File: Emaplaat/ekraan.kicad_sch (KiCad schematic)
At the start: 37 parts, among them IC1 74HC595PW-Q100,118, IC10 1EDN7550BXTSA1, IC11 1EDN7550BXTSA1, IC3 1EDN7550BXTSA1, IC6 1EDN7550BXTSA1, IC7 1EDN7550BXTSA1, IC8 1EDN7550BXTSA1, IC9 1EDN7550BXTSA1, U1 1EDN7550BXTSA1

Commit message: qwerghhgfdsdfghqwerghhgfdsdfghjj
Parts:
- removed C1, C16, C18, C2, C5, C6, C9: 22u, symbol Device:C
- removed C15, C17, C19, C3, C4, C7, C8: 20u, Capacitor_SMD:C_0201_0603Metric, symbol Device:C
- removed IC10, IC11, IC3, IC6, IC7, IC8, IC9: 1EDN7550BXTSA1, SOT95P280X145-6N, symbol 1EDN7550BXTSA1:1EDN7550BXTSA1
- removed R10, R11, R12, R13, R14, R15, R16, R17, R3, R4, R9: 33k, symbol Device:R
- removed U1: 1EDN7550BXTSA1, dot_flipper:7_flip_dots, symbol flipdot_7xarray:flipdot_7xarray
- added C31, C33, C35, C37, C39, C41, C49, C51, C53, C55, C57, C59: 47u, symbol Device:C
- added C32, C34, C36, C38, C40, C42, C50, C52, C54, C56, C58, C60: 100u, symbol Device:C
- added IC11, IC12, IC13, IC14, IC15, IC17, IC18, IC19, IC20, IC21, IC22: 74HC595PW-Q100,118, SOP65P640X110-16N, symbol 74HC595PW-Q100_118:74HC595PW-Q100,118
- added R21, R22: 10k, symbol Device:R
- R18, R19, R20: value 33k -> 10k
- renumbered IC1 to IC10
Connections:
- net 1D+ is gone; now on net DS: R18.2
- net 1E+ is gone; now on net SHCP: R20.2
- net 1E- is gone; now on net STCP: R19.2
- net 3V3: now also C31.1, C32.1, C33.1, C34.1, C35.1, C36.1, C37.1, C38.1, C39.1, C40.1, C41.1, C42.1, C49.1, C50.1, C51.1, C52.1, C53.1, C54.1, C55.1, C56.1, C57.1, C58.1, C59.1, C60.1, IC11.16 (VCC), IC12.16 (VCC), IC13.16 (VCC), IC14.16 (VCC), IC15.16 (VCC), IC17.16 (VCC), IC18.16 (VCC), IC19.16 (VCC), IC20.16 (VCC), IC21.16 (VCC), IC22.16 (VCC), R21.2, R22.2
- net AGND: now also R18.1, R19.1, R20.1, C31.2, C32.2, C33.2, C34.2, C35.2, C36.2, C37.2, C38.2, C39.2, C40.2, C41.2, C42.2, C49.2, C50.2, C51.2, C52.2, C53.2, C54.2, C55.2, C56.2, C57.2, C58.2, C59.2, C60.2, IC11.8 (GND), IC12.8 (GND), IC13.8 (GND), IC14.8 (GND), IC15.8 (GND), IC17.8 (GND), IC18.8 (GND), IC19.8 (GND), IC20.8 (GND), IC21.8 (GND), IC22.8 (GND), IC22.9 (Q7S)
- net 1-: now reaches IC10.1 (Q1)
- net !MR: now reaches IC10.10 (~{MR})
- net !MR: now also IC11.10 (~{MR}), IC12.10 (~{MR}), IC13.10 (~{MR}), IC14.10 (~{MR}), IC15.10 (~{MR}), IC17.10 (~{MR}), IC18.10 (~{MR}), IC19.10 (~{MR}), IC20.10 (~{MR}), IC21.10 (~{MR}), IC22.10 (~{MR}), R21.1
- net SHCP: now reaches IC10.11 (SHCP)
- net SHCP: now also IC11.11 (SHCP), IC12.11 (SHCP), IC13.11 (SHCP), IC14.11 (SHCP), IC15.11 (SHCP), IC17.11 (SHCP), IC18.11 (SHCP), IC19.11 (SHCP), IC20.11 (SHCP), IC21.11 (SHCP), IC22.11 (SHCP)
- net STCP: now reaches IC10.12 (STCP)
- net STCP: now also IC11.12 (STCP), IC12.12 (STCP), IC13.12 (STCP), IC14.12 (STCP), IC15.12 (STCP), IC17.12 (STCP), IC18.12 (STCP), IC19.12 (STCP), IC20.12 (STCP), IC21.12 (STCP), IC22.12 (STCP)
- net !OE: now reaches IC10.13 (~{OE})
- net !OE: now also IC11.13 (~{OE}), IC12.13 (~{OE}), IC13.13 (~{OE}), IC14.13 (~{OE}), IC15.13 (~{OE}), IC17.13 (~{OE}), IC18.13 (~{OE}), IC19.13 (~{OE}), IC20.13 (~{OE}), IC21.13 (~{OE}), IC22.13 (~{OE}), R22.1
- net DS: now reaches IC10.14 (DS)
- net 1+: now reaches IC10.15 (Q0)
- net 2+: now reaches IC10.2 (Q2)
- net 2-: now reaches IC10.3 (Q3)
- net 3+: now reaches IC10.4 (Q4)
- net 3-: now reaches IC10.5 (Q5)
- net 4+: now reaches IC10.6 (Q6)
- net 4-: now reaches IC10.7 (Q7)
- net at IC10.9 (Q7S): now also IC13.14 (DS)
- new net: IC14.9 (Q7S), IC18.14 (DS)
- new net: IC18.9 (Q7S), IC21.14 (DS)
- new net: IC11.9 (Q7S), IC14.14 (DS)
- new net: IC13.9 (Q7S), IC17.14 (DS)
- new net: IC17.9 (Q7S), IC20.14 (DS)
- new net: IC12.14 (DS), IC21.9 (Q7S)
- new net: IC12.9 (Q7S), IC15.14 (DS)
- new net: IC15.9 (Q7S), IC19.14 (DS)
- new net: IC19.9 (Q7S), IC22.14 (DS)
- new net: IC11.14 (DS), IC20.9 (Q7S)
- new net 10+: IC11.2 (Q2)
- new net 10-: IC11.3 (Q3)
- new net 11+: IC11.4 (Q4)
- new net 11-: IC11.5 (Q5)
- new net 12+: IC11.6 (Q6)
- new net 12-: IC11.7 (Q7)
- new net 13+: IC14.15 (Q0)
- new net 13-: IC14.1 (Q1)
- new net 14+: IC14.2 (Q2)
- new net 14-: IC14.3 (Q3)
- new net 15+: IC14.4 (Q4)
- new net 15-: IC14.5 (Q5)
- new net 16+: IC14.6 (Q6)
- new net 16-: IC14.7 (Q7)
- new net 17+: IC12.15 (Q0)
- new net 17-: IC12.1 (Q1)
- new net 18+: IC12.2 (Q2)
- new net 18-: IC12.3 (Q3)
- new net 19+: IC12.4 (Q4)
- new net 19-: IC12.5 (Q5)
- new net 20+: IC12.6 (Q6)
- new net 20-: IC12.7 (Q7)
- new net 21+: IC15.15 (Q0)
- new net 21-: IC15.1 (Q1)
- new net 22+: IC15.2 (Q2)
- new net 22-: IC15.3 (Q3)
- new net 23+: IC15.4 (Q4)
- new net 23-: IC15.5 (Q5)
- new net 24+: IC15.6 (Q6)
- new net 24-: IC15.7 (Q7)
- new net 25+: IC17.15 (Q0)
- new net 25-: IC17.1 (Q1)
- new net 26+: IC17.2 (Q2)
- new net 26-: IC17.3 (Q3)
- new net 27+: IC17.4 (Q4)
- new net 27-: IC17.5 (Q5)
- new net 28+: IC17.6 (Q6)
- new net 28-: IC17.7 (Q7)
- new net 29+: IC20.15 (Q0)
- new net 29-: IC20.1 (Q1)
- new net 30+: IC20.2 (Q2)
- new net 30-: IC20.3 (Q3)
- new net 31+: IC20.4 (Q4)
- new net 31-: IC20.5 (Q5)
- new net 32+: IC20.6 (Q6)
- new net 32-: IC20.7 (Q7)
- new net 33+: IC18.15 (Q0)
- new net 33-: IC18.1 (Q1)
- new net 34+: IC18.2 (Q2)
- new net 34-: IC18.3 (Q3)
- new net 35+: IC18.4 (Q4)
- new net 35-: IC18.5 (Q5)
- new net 36+: IC18.6 (Q6)
- new net 36-: IC18.7 (Q7)
- new net 37+: IC21.15 (Q0)
- new net 37-: IC21.1 (Q1)
- new net 38+: IC21.2 (Q2)
- new net 38-: IC21.3 (Q3)
- new net 39+: IC21.4 (Q4)
- new net 39-: IC21.5 (Q5)
- new net 40+: IC21.6 (Q6)
- new net 40-: IC21.7 (Q7)
- new net 41+: IC19.15 (Q0)
- new net 41-: IC19.1 (Q1)
- new net 42+: IC19.2 (Q2)
- new net 42-: IC19.3 (Q3)
- new net 43+: IC19.4 (Q4)
- new net 43-: IC19.5 (Q5)
- new net 44+: IC19.6 (Q6)
- new net 44-: IC19.7 (Q7)
- new net 45+: IC22.15 (Q0)
- new net 45-: IC22.1 (Q1)
- new net 46+: IC22.2 (Q2)
- new net 46-: IC22.3 (Q3)
- new net 47+: IC22.4 (Q4)
- new net 47-: IC22.5 (Q5)
- new net 48+: IC22.6 (Q6)
- new net 48-: IC22.7 (Q7)
- new net 5+: IC13.15 (Q0)
- new net 5-: IC13.1 (Q1)
- new net 6+: IC13.2 (Q2)
- new net 6-: IC13.3 (Q3)
- new net 7+: IC13.4 (Q4)
- new net 7-: IC13.5 (Q5)
- new net 8+: IC13.6 (Q6)
- new net 8-: IC13.7 (Q7)
- new net 9+: IC11.15 (Q0)
- new net 9-: IC11.1 (Q1)
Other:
- added sheet array (array.kicad_sch)
- added sheet array1 (array.kicad_sch)
- added sheet array2 (array.kicad_sch)
- added sheet array3 (array.kicad_sch)
- added sheet array4 (array.kicad_sch)
- added sheet array5 (array.kicad_sch)
- added sheet array6 (array.kicad_sch)
- note added: "!MR ja !OE tõmmatud üles, ülejäänud sisendid tõmmatud alla"
- note added: "6 nihkeregistrit kontrollimaks 48 flipdot-i"
- note added: "7x7 flipdot-i"
- moved on the sheet: IC10

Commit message: ketamine addict
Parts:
- removed R18, R19, R20, R21, R22: 10k, symbol Device:R
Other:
- sheet array ports: added none; removed 12V, PGND
- sheet array1 ports: added none; removed 12V, PGND
- sheet array2 ports: added none; removed 12V, PGND
- sheet array3 ports: added none; removed 12V, PGND
- sheet array4 ports: added none; removed 12V, PGND
- sheet array5 ports: added none; removed 12V, PGND
- sheet array6 ports: added none; removed 12V, PGND
- note added: "ühendused"
- note removed: "!MR ja !OE tõmmatud üles, ülejäänud sisendid tõmmatud alla"
- moved on the sheet: C31, C32, C33, C34, C35, C36, C37, C38, C39, C40, C41, C42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

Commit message: T________T Heiki Tammemägi
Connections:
- net AGND renamed GND

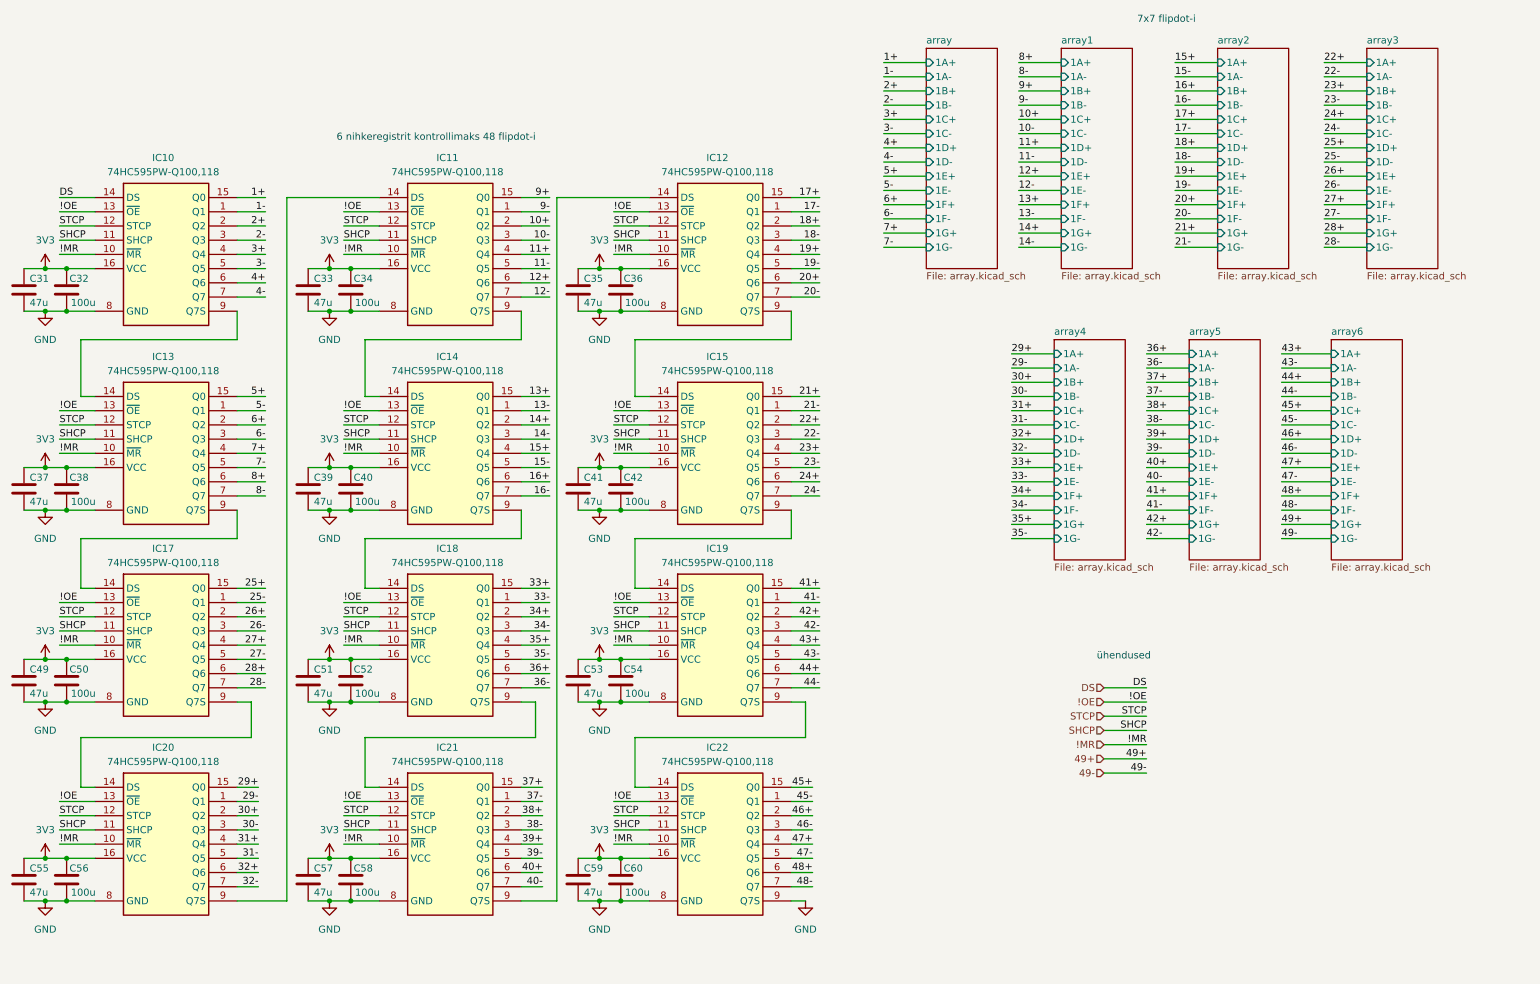
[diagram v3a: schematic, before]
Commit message: skeem v2 kinda valmis, simulatsioon ka tehtud
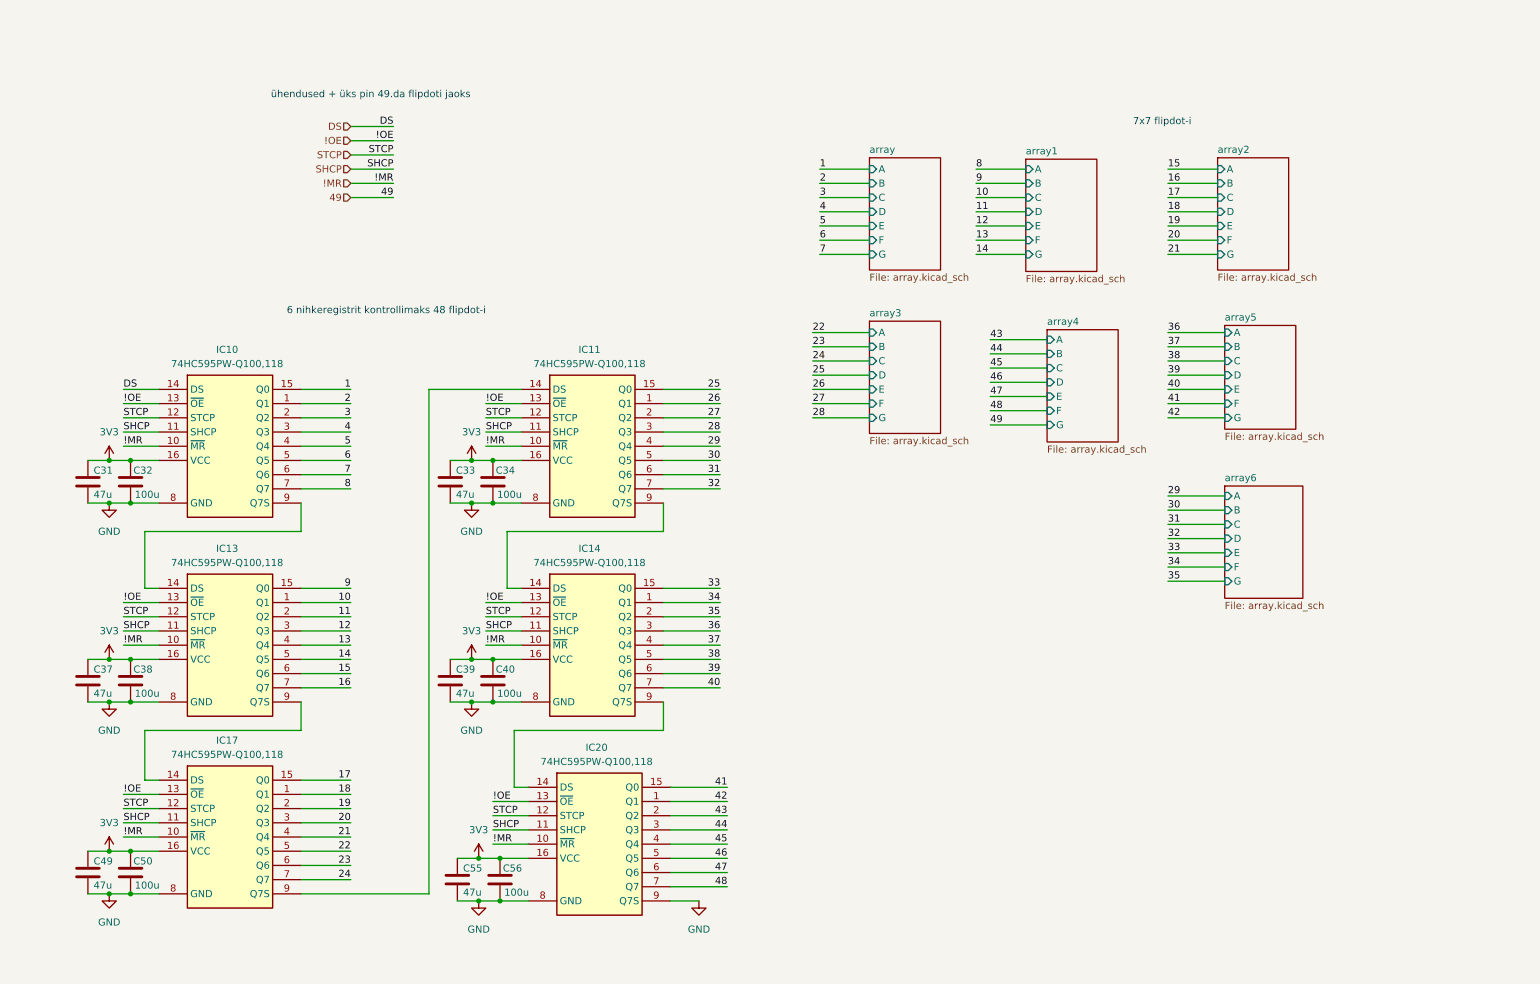
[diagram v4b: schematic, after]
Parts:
- removed C35, C41, C51, C53, C57, C59: 47u, symbol Device:C
- removed C36, C42, C52, C54, C58, C60: 100u, symbol Device:C
- removed IC12, IC15, IC18, IC19, IC21, IC22: 74HC595PW-Q100,118, SOP65P640X110-16N, symbol 74HC595PW-Q100_118:74HC595PW-Q100,118
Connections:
- net GND: now also IC20.9 (Q7S)
- net at IC14.9 (Q7S): now also IC20.14 (DS)
- net at IC17.9 (Q7S): now also IC11.14 (DS); no longer IC20.14 (DS)
- net 1+ renamed 1
- net 1- renamed 2
- net 10+ renamed 27
- net 10- renamed 28
- net 11+ renamed 29
- net 11- renamed 30
- net 12+ renamed 31
- net 12- renamed 32
- net 13+ renamed 33
- net 13- renamed 34
- net 14+ renamed 35
- net 14- renamed 36
- net 15+ renamed 37
- net 15- renamed 38
- net 16+ renamed 39
- net 16- renamed 40
- net 2+ renamed 3
- net 2- renamed 4
- net 25+ renamed 17
- net 25- renamed 18
- net 26+ renamed 19
- net 26- renamed 20
- net 27+ renamed 21
- net 27- renamed 22
- net 28+ renamed 23
- net 28- renamed 24
- net 29+ renamed 41
- net 29- renamed 42
- net 3+ renamed 5
- net 3- renamed 6
- net 30+ renamed 43
- net 30- renamed 44
- net 31+ renamed 45
- net 31- renamed 46
- net 32+ renamed 47
- net 32- renamed 48
- net 4+ renamed 7
- net 4- renamed 8
- net 5+ renamed 9
- net 5- renamed 10
- net 6+ renamed 11
- net 6- renamed 12
- net 7+ renamed 13
- net 7- renamed 14
- net 8+ renamed 15
- net 8- renamed 16
- net 9+ renamed 25
- net 9- renamed 26
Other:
- sheet array ports: added A, B, C, D, E, F, G; removed 1A+, 1A-, 1B+, 1B-, 1C+, 1C-, 1D+, 1D-, 1E+, 1E-, 1F+, 1F-, 1G+, 1G-
- sheet array1 ports: added A, B, C, D, E, F, G; removed 1A+, 1A-, 1B+, 1B-, 1C+, 1C-, 1D+, 1D-, 1E+, 1E-, 1F+, 1F-, 1G+, 1G-
- sheet array2 ports: added A, B, C, D, E, F, G; removed 1A+, 1A-, 1B+, 1B-, 1C+, 1C-, 1D+, 1D-, 1E+, 1E-, 1F+, 1F-, 1G+, 1G-
- sheet array3 ports: added A, B, C, D, E, F, G; removed 1A+, 1A-, 1B+, 1B-, 1C+, 1C-, 1D+, 1D-, 1E+, 1E-, 1F+, 1F-, 1G+, 1G-
- sheet array4 ports: added A, B, C, D, E, F, G; removed 1A+, 1A-, 1B+, 1B-, 1C+, 1C-, 1D+, 1D-, 1E+, 1E-, 1F+, 1F-, 1G+, 1G-
- sheet array5 ports: added A, B, C, D, E, F, G; removed 1A+, 1A-, 1B+, 1B-, 1C+, 1C-, 1D+, 1D-, 1E+, 1E-, 1F+, 1F-, 1G+, 1G-
- sheet array6 ports: added A, B, C, D, E, F, G; removed 1A+, 1A-, 1B+, 1B-, 1C+, 1C-, 1D+, 1D-, 1E+, 1E-, 1F+, 1F-, 1G+, 1G-
- note added: "ühendused + üks pin 49.da flipdoti jaoks"
- note removed: "ühendused"
- moved on the sheet: C31, C32, C33, C34, C37, C38, C39, C40, C49, C50, C55, C56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

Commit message: fsfsfe
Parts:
- removed C32, C34, C38, C40, C50, C56: 100u, symbol Device:C
- removed C49, C55: 47u, symbol Device:C
- added C16, C35: 100n, symbol Device:C
- C31, C33, C37, C39: value 47u -> 100n
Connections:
- net 3V3: now also C16.1, C35.1
- net GND: now also C16.2, C35.2
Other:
- note added: "6 nihkeregistrit kontrollimaks 48 flipdot-i, bypass kondekad võetud 6. videoloeng 29min juures"
- note removed: "6 nihkeregistrit kontrollimaks 48 flipdot-i"
